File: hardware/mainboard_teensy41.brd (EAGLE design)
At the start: 69.9 x 100.3 mm, 195 parts, among them IC1 ATMEGA328-20P, IC2 7805TV, Q1 2N3904, Q2 2N3904, Q3 2N3904, Q4 2N3904, Q5 2N3904, Q6 2N3904

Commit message: Created custom SPISlave class to use 2 pins only
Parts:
- R1: value (none) -> 620R
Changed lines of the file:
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@@
 <attribute name="VALUE" x="18.542" y="40.9702" size="1.778" layer="27" ratio="10"/>
 </element>
-<element name="R1" library="resistors" package="RESISTOR/7.5" value="" x="27.94" y="26.67" smashed="yes" rot="R270">
+<element name="R1" library="resistors" package="RESISTOR/7.5" value="620R" x="27.94" y="26.67" smashed="yes" rot="R270">
 <attribute name="NAME" x="27.432" y="29.21" size="1.016" layer="25" ratio="10" rot="R270"/>
 <attribute name="VALUE" x="29.2862" y="29.591" size="1.27" layer="27" ratio="10" rot="R270"/>

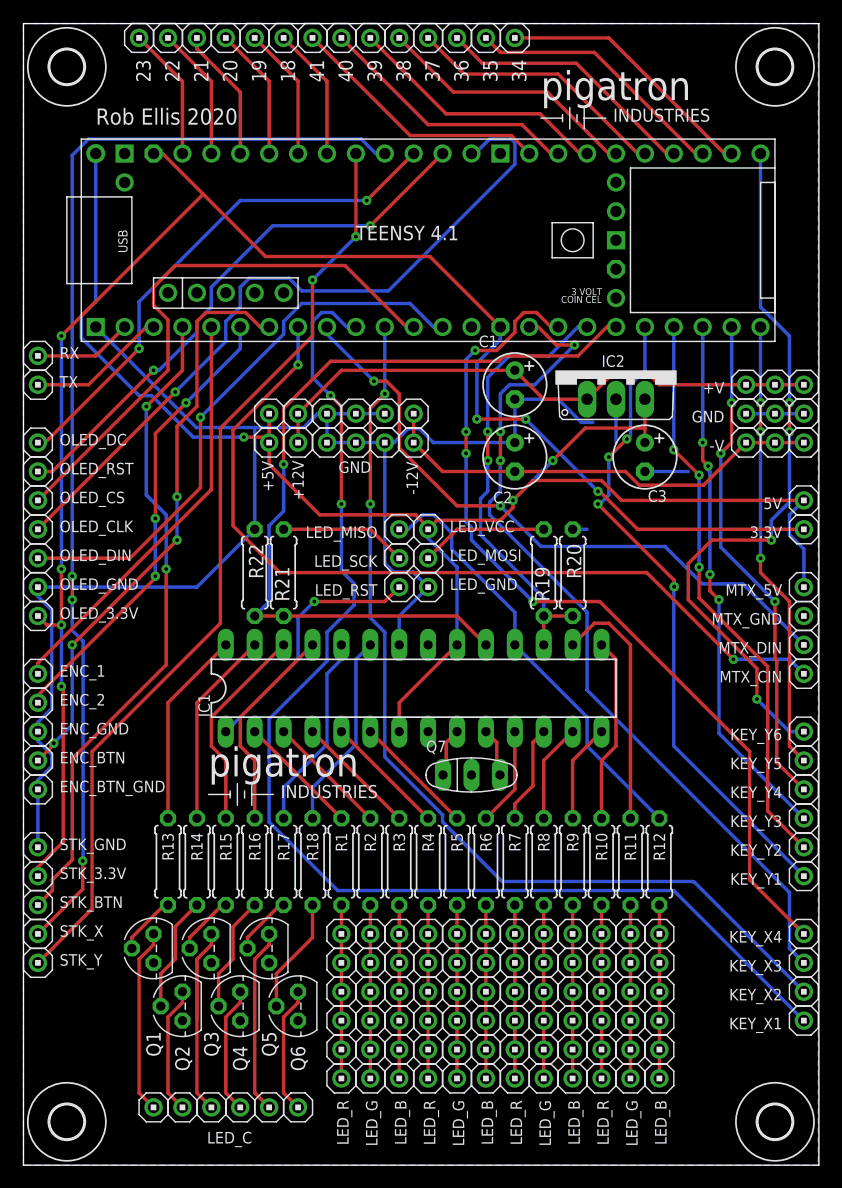
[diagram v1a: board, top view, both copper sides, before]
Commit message: Use serial to communicate with keyboard led driver
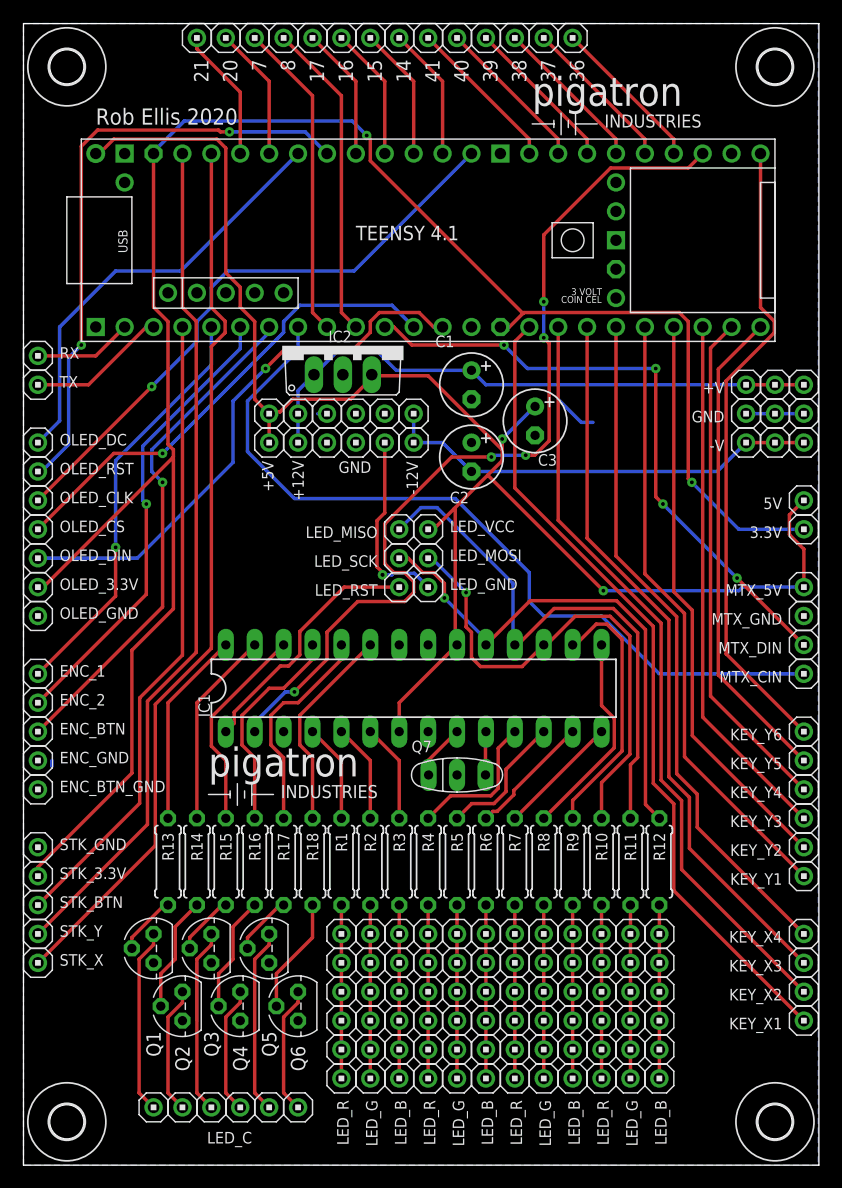
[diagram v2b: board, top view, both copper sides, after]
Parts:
- removed 22, 23, 34, 35: HEADER/MALE/01, connectors:HEADER/MALE/01
- removed R19, R21: 1k, resistors:RESISTOR/7.5
- removed R20, R22: 2k, resistors:RESISTOR/7.5
- added 14, 15, 16, 17: HEADER/MALE/01, connectors:HEADER/MALE/01
- R1: value 620R -> 510R
- R10, R11, R12, R2, R3, R4, R5, R6, R7, R8, R9: value (none) -> 510R
- moved IC2 24.1 mm to (28.1, 72.0)
- moved C3 10.2 mm to (45.0, 65.4)
- moved 41 10.2 mm to (35.6, 99.1)
- moved 39 10.2 mm to (40.6, 99.1)
- moved 40 10.2 mm to (38.1, 99.1)
- moved 36 10.2 mm to (48.3, 99.1)
- moved 37 10.2 mm to (45.7, 99.1)
- moved 38 10.2 mm to (43.2, 99.1)
- moved C1 3.81 mm to (39.4, 68.6)
- moved C2 3.81 mm to (39.4, 62.2)
- moved ENC_BTN 2.54 mm to (1.27, 38.1)
- moved ENC_GND 2.54 mm to (1.27, 35.6)
- moved OLED_3.3V 2.54 mm to (1.27, 50.8)
- moved OLED_CLK 2.54 mm to (1.27, 58.4)
- moved OLED_CS 2.54 mm to (1.27, 55.9)
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- renumbered 18 to 8, 19 to 7
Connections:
- removed net LED_MOSI: IC1.17, R19.1, R20.2, U$1.26-A12/MOSI1
- removed net LED_SCK: IC1.19, R21.1, R22.2, U$1.27-A13/SCK1
- removed net N$78: 23.1, U$1.23-A9/CRX1/MCLK1
- removed net N$85: LED_MOSI.1, R19.2
- new net LED_DATA: IC1.2, U$1.35-TX8
- net GND: no longer R20.1, R22.1
- net N$1: now also IC1.4; no longer IC1.2
- net N$12: now also KEY_X3.1, U$1.26-A12/MOSI1; no longer KEY_X2.1, U$1.9-OUT1C
- net N$21: now also U$1.27-A13/SCK1; no longer U$1.25-A11/RX6/SDA2
- net N$22: now also STK_X.1, U$1.22-A8/CTX1; no longer KEY_X3.1, U$1.24-A10/TX6/SCL2
- net N$23: now also U$1.23-A9/CRX1/MCLK1; no longer U$1.17-A3/TX4/SDA1
- net N$24: now also OLED_RST.1, U$1.18-A4/SDA0; no longer STK_X.1, U$1.16-A2/RX4/SCL1
- net N$25: now also U$1.19-A5/SCL0; no longer U$1.15-A1/RX3/SPDIF_IN
- net N$26: now also 14.1; no longer OLED_RST.1
- net N$27: now also IC1.5; no longer IC1.3
- net N$28: now also IC1.6; no longer IC1.4
- net N$29: now also IC1.11; no longer IC1.5
- net N$30: now also IC1.12; no longer IC1.6
- net N$31: now also IC1.13; no longer IC1.11
- net N$32: now also IC1.14; no longer IC1.12
- net N$33: now also IC1.15; no longer IC1.13
- net N$34: now also IC1.16; no longer IC1.14
- net N$35: now also IC1.17, LED_MOSI.1; no longer IC1.15
- net N$36: now also IC1.18, LED_MISO.1; no longer IC1.16
- net N$37: now also 15.1, U$1.15-A1/RX3/SPDIF_IN; no longer IC1.18, LED_MISO.1, R12.1
- net N$7: now also KEY_X1.1, U$1.24-A10/TX6/SCL2; no longer MTX_DIN.1, U$1.7-RX2/OUT1A
- net N$71: now also 16.1, U$1.16-A2/RX4/SCL1; no longer 34.1, U$1.34-RX8
- net N$72: now also 17.1, U$1.17-A3/TX4/SDA1; no longer 35.1, U$1.35-TX8
- net N$73: now also 7.1, U$1.7-RX2/OUT1A; no longer 8.1, U$1.18-A4/SDA0
- net N$74: now also 8.1, U$1.8-TX2/IN1; no longer 7.1, U$1.19-A5/SCL0
- net N$77: now also MTX_DIN.1, U$1.9-OUT1C; no longer 22.1, U$1.22-A8/CTX1
- net N$8: now also KEY_X2.1, U$1.25-A11/RX6/SDA2; no longer KEY_X1.1, U$1.8-TX2/IN1
- net N$86: now also IC1.19, R12.1; no longer R21.2
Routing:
- net GND: track 156.6 -> 32.1 mm, vias 0 -> 1
- net LED_DATA: track 0.00 -> 81.2 mm, vias 0 -> 5
- net LED_SCK: track 72.8 -> 0.00 mm, vias 1 -> 0
- net N$24: track 99.0 -> 53.4 mm, vias 3 -> 2
- net N$77: track 11.7 -> 55.0 mm, vias 0 -> 4
- net N$8: track 107.5 -> 67.4 mm, vias 2 -> 0
- net LED_MOSI: track 39.2 -> 0.00 mm, vias 2 -> 0
- net N$26: track 48.7 -> 11.7 mm, vias 2 -> 0
- net N$86: track 11.2 -> 45.6 mm, vias 0 -> 1
- net N$35: track 16.3 -> 44.3 mm, vias 0 -> 1
- net N$37: track 38.4 -> 11.7 mm
- net N$36: track 21.9 -> 48.6 mm
- net 3.3V: track 147.0 -> 170.8 mm, vias 7 -> 2
- net N$12: track 84.6 -> 63.8 mm, vias 2 -> 0
- net N$21: track 77.1 -> 60.2 mm, vias 4 -> 0
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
